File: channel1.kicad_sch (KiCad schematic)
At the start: 33 parts

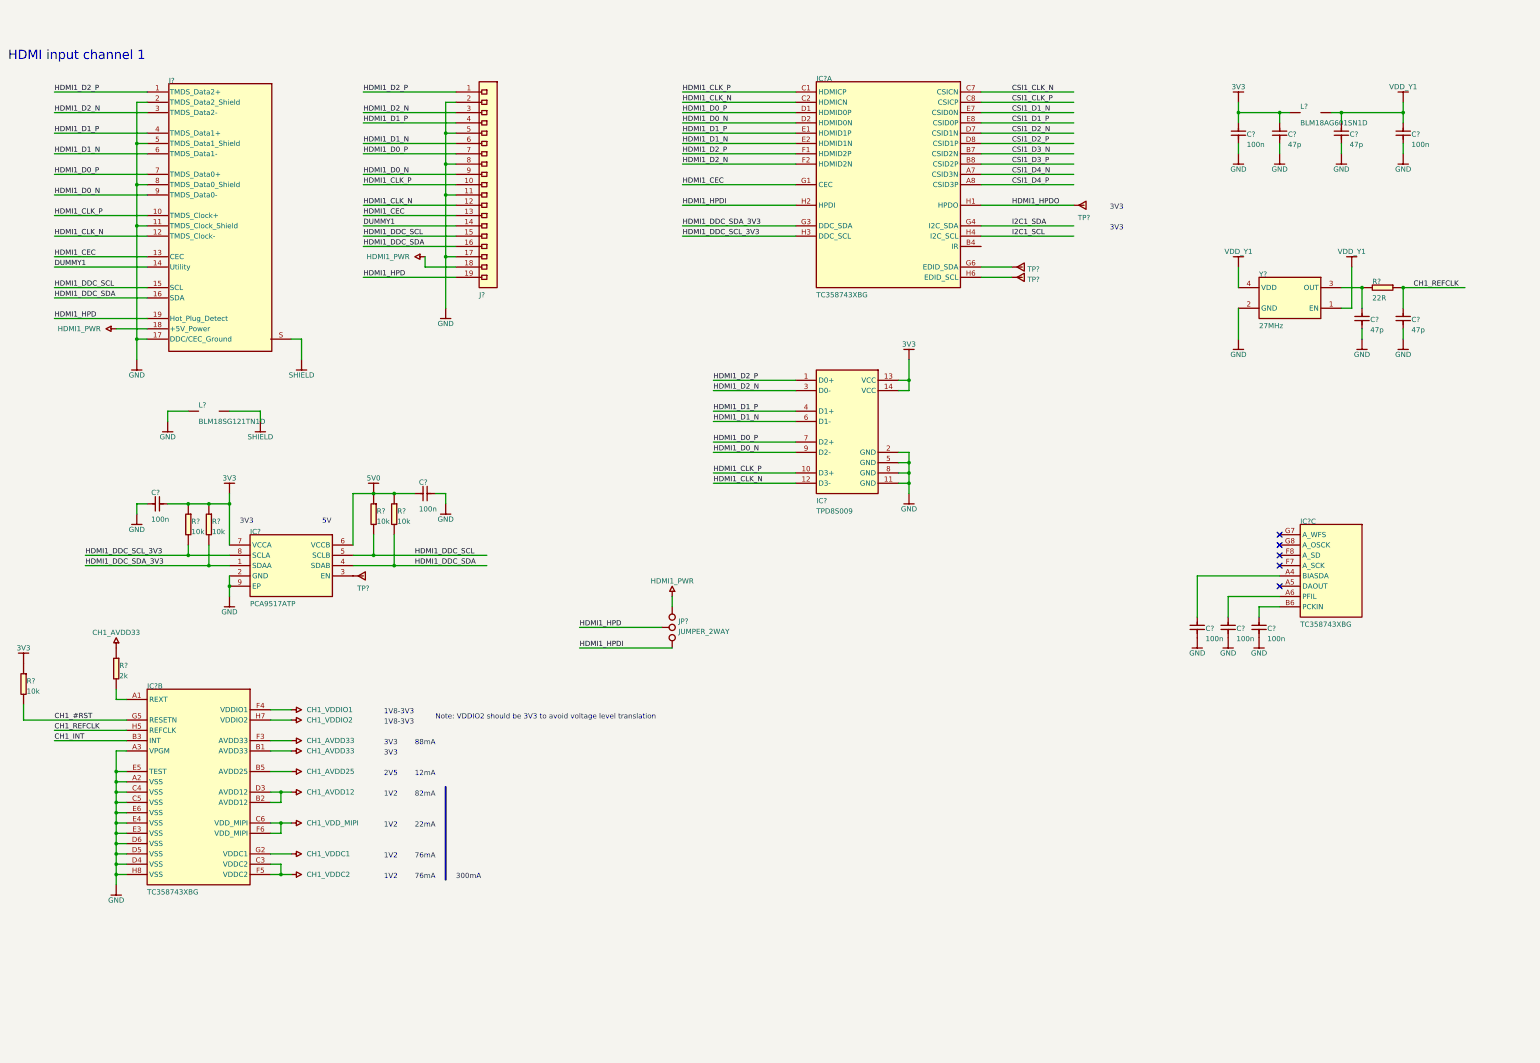
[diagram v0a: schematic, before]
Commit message: Change components to antmicro library ones
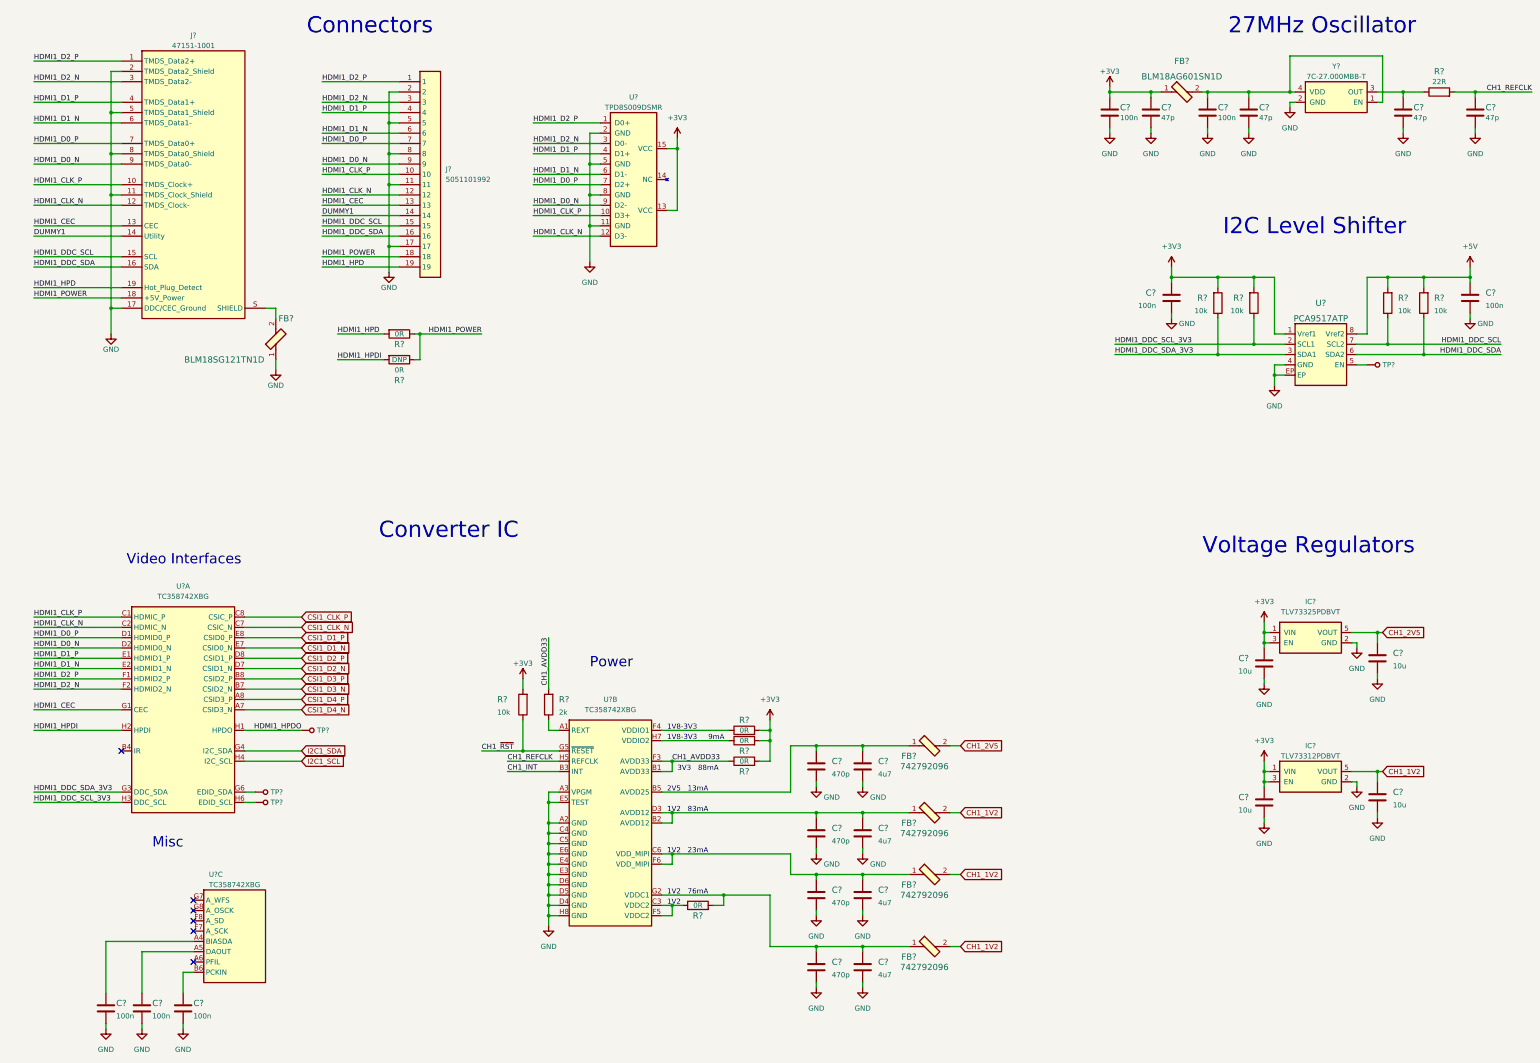
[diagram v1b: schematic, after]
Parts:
- removed C? (x9): ${ALTIUM_VALUE}, HDMI-MIPI-Bridge.Pcblib:0402, symbol altium_import-altium-import:1_C
- removed C? (x2): ${ALTIUM_VALUE}, HDMI-MIPI-Bridge.Pcblib:0402, symbol altium_import-altium-import:2_C
- removed IC? (x3): ${ALTIUM_VALUE}, HDMI-MIPI-Bridge.Pcblib:TC358743XBG, symbol altium_import-altium-import:0_TC358743XBG
- removed IC?: ${ALTIUM_VALUE}, HDMI-MIPI-Bridge.Pcblib:PCA9517ATP, symbol altium_import-altium-import:0_PCA9517ATP
- removed IC?: ${ALTIUM_VALUE}, HDMI-MIPI-Bridge.Pcblib:SON-15, symbol altium_import-altium-import:0_TPD8S009
- removed J?: ${ALTIUM_VALUE}, HDMI-MIPI-Bridge.Pcblib:Molex_HDMI_471511001, symbol altium_import-altium-import:0_CON-Molex-471511001
- removed J?: ${ALTIUM_VALUE}, HDMI-MIPI-Bridge.Pcblib:CON-Molex-505110-1992, symbol altium_import-altium-import:0_1X19
- removed JP?: JUMPER_2WAY, HDMI-MIPI-Bridge.Pcblib:JUMPER_2WAY, symbol altium_import-altium-import:3_JUMPER_2WAY
- removed L? (x2): ${ALTIUM_VALUE}, HDMI-MIPI-Bridge.Pcblib:0603, symbol altium_import-altium-import:0_Inductor SMT
- removed R?: ${ALTIUM_VALUE}, HDMI-MIPI-Bridge.Pcblib:0603, symbol altium_import-altium-import:1_R
- removed R? (x5): ${ALTIUM_VALUE}, HDMI-MIPI-Bridge.Pcblib:0402, symbol altium_import-altium-import:1_R
- removed R?: ${ALTIUM_VALUE}, HDMI-MIPI-Bridge.Pcblib:0402, symbol altium_import-altium-import:0_R
- removed TP? (x4): Testpad, HDMI-MIPI-Bridge.Pcblib:TP-R-1, symbol altium_import-altium-import:3_Testpad
- removed Y?: ${ALTIUM_VALUE}, HDMI-MIPI-Bridge.Pcblib:TXC_7C, symbol altium_import-altium-import:0_TXC_7C
- added C? (x4): C_4u7_0603, antmicro-footprints:0603-cap, symbol antmicroCapacitors0603:C_4u7_0603
- added C? (x4): C_470p_0402, antmicro-footprints:0402-cap, symbol antmicroCapacitors0402:C_470p_0402
- added C? (x4): C_10u_0603, antmicro-footprints:0603-cap, symbol antmicroCapacitors0603:C_10u_0603
- added C? (x7): C_100n_0402, antmicro-footprints:0402-cap, symbol antmicroCapacitors0402:C_100n_0402
- added C? (x4): C_47p_0402, antmicro-footprints:0402-cap, symbol antmicroCapacitors0402:C_47p_0402
- added FB? (x4): 742792096, antmicro-footprints:0805-res, symbol antmicroFerriteBeadsandChips:742792096
- added FB?: BLM18SG121TN1D, antmicro-footprints:0603-res, symbol antmicroFerriteBeadsandChips:BLM18SG121TN1D
- added FB?: BLM18AG601SN1D, antmicro-footprints:0603, symbol antmicroFerriteBeadsandChips:BLM18AG601SN1D
- added IC?: TLV73312PDBVT, antmicro-footprints:SOT-23-5, symbol antmicroPMICVoltageRegulatorsLinear:TLV73312PDBVT
- added IC?: TLV73325PDBVT, antmicro-footprints:SOT-23-5, symbol antmicroPMICVoltageRegulatorsLinear:TLV73325PDBVT
- added J?: 5051101992, antmicro-footprints:5051101992, symbol antmicroFCCConnectors:5051101992
- added J?: 47151-1001, antmicro-footprints:47151-1001, symbol antmicroUSBDVIHDMIConnectors:47151-1001
- added R? (x5): R_10k_0402, antmicro-footprints:0402-res, symbol antmicroResistors0402:R_10k_0402
- added R? (x6): R_0R_0603, antmicro-footprints:0603-res, symbol antmicroResistors0603:R_0R_0603
- added R?: R_22R_0402, antmicro-footprints:0402-res, symbol antmicroResistors0402:R_22R_0402
- added R?: R_2k_0402, antmicro-footprints:0402-res, symbol antmicroResistors0402:R_2k_0402
- added TP? (x4): TP_SMD_0_75MM, antmicro-footprints:Testpoint_smd_0_75mm, symbol antmicroTestPoints:TP_SMD_0_75MM
- added U?: TPD8S009DSMR, antmicro-footprints:R-PDSO-N15, symbol antmicroTVSDiodes:TPD8S009DSMR
- added U?: PCA9517ATP, antmicro-footprints:SOT1069-2, symbol antmicroLogicTranslatorsLevelShifters:PCA9517ATP
- added U? (x3): TC358742XBG, antmicro-footprints:BGA-64_8x8_6.0x6.0mm, symbol antmicroInterfaceControllers:TC358742XBG
- added Y?: 7C-27.000MBB-T, antmicro-footprints:7C-24.000MBB-T, symbol antmicroOscillators:7C-27.000MBB-T
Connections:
- net CH1_AVDD33: now also R?.1, R?.2, U?.B1 (AVDD33), U?.F3 (AVDD33)
- net CH1_INT: now also U?.B3 (INT)
- net CH1_REFCLK: now also C?.1, R?.2, U?.H5 (REFCLK)
- net CSI1_CLK_N: now also U?.C7 (CSIC_N)
- net CSI1_CLK_P: now also U?.C8 (CSIC_P)
- net CSI1_D1_N: now also U?.E7 (CSID0_N)
- net CSI1_D1_P: now also U?.E8 (CSID0_P)
- net CSI1_D2_N: now also U?.D7 (CSID1_N)
- net CSI1_D2_P: now also U?.D8 (CSID1_P)
- net CSI1_D3_N: now also U?.B7 (CSID2_N)
- net CSI1_D3_P: now also U?.B8 (CSID2_P)
- net CSI1_D4_N: now also U?.A7 (CSID3_N)
- net CSI1_D4_P: now also U?.A8 (CSID3_P)
- net DUMMY1: now also J?.14, J?.14 (Utility)
- net GND: now also C?.1, C?.1, C?.1, C?.1, C?.2, C?.2, C?.2, C?.2, C?.2, C?.2, C?.2, C?.2, C?.2, C?.2, C?.2, C?.2, C?.2, C?.2, C?.2, C?.2, C?.2, C?.2, C?.2, FB?.1, IC?.2 (GND), IC?.2 (GND), J?.11, J?.11 (TMDS_Clock_Shield), J?.17, J?.17 (DDC/CEC_Ground), J?.2, J?.2 (TMDS_Data2_Shield), J?.5, J?.5 (TMDS_Data1_Shield), J?.8, J?.8 (TMDS_Data0_Shield), U?.11 (GND), U?.2 (GND), U?.4 (GND), U?.5 (GND), U?.8 (GND), U?.A2 (GND), U?.A3 (VPGM), U?.C4 (GND), U?.C5 (GND), U?.D4 (GND), U?.D5 (GND), U?.D6 (GND), U?.E3 (GND), U?.E4 (GND), U?.E5 (TEST), U?.E6 (GND), U?.EP, U?.H8 (GND), Y?.2 (GND)
- net HDMI1_CEC: now also J?.13, J?.13 (CEC), U?.G1 (CEC)
- net HDMI1_CLK_N: now also J?.12, J?.12 (TMDS_Clock-), U?.12 (D3-), U?.C2 (HDMIC_N)
- net HDMI1_CLK_P: now also J?.10, J?.10 (TMDS_Clock+), U?.10 (D3+), U?.C1 (HDMIC_P)
- net HDMI1_D0_N: now also J?.9, J?.9 (TMDS_Data0-), U?.9 (D2-), U?.D2 (HDMID0_N)
- net HDMI1_D0_P: now also J?.7, J?.7 (TMDS_Data0+), U?.7 (D2+), U?.D1 (HDMID0_P)
- net HDMI1_D1_N: now also J?.6, J?.6 (TMDS_Data1-), U?.6 (D1-), U?.E2 (HDMID1_N)
- net HDMI1_D1_P: now also J?.4, J?.4 (TMDS_Data1+), U?.4 (D1+), U?.E1 (HDMID1_P)
- net HDMI1_D2_N: now also J?.3, J?.3 (TMDS_Data2-), U?.3 (D0-), U?.F2 (HDMID2_N)
- net HDMI1_D2_P: now also J?.1, J?.1 (TMDS_Data2+), U?.1 (D0+), U?.F1 (HDMID2_P)
- net HDMI1_DDC_SCL: now also J?.15, J?.15 (SCL), R?.1, U?.7 (SCL2)
- net HDMI1_DDC_SCL_3V3: now also R?.1, U?.2 (SCL1), U?.H3 (DDC_SCL)
- net HDMI1_DDC_SDA: now also J?.16, J?.16 (SDA), R?.1, U?.6 (SDA2)
- net HDMI1_DDC_SDA_3V3: now also R?.1, U?.3 (SDA1), U?.G3 (DDC_SDA)
- net HDMI1_HPD: now also J?.19, J?.19 (Hot_Plug_Detect), R?.2
- net HDMI1_HPDI: now also R?.2, U?.H2 (HPDI)
- net HDMI1_HPDO: now also TP?.1, U?.H1 (HPDO)
- net I2C1_SCL: now also U?.H4 (I2C_SCL)
- net I2C1_SDA: now also U?.G4 (I2C_SDA)
- new net: C?.1, C?.2, FB?.1, U?.C6 (VDD_MIPI), U?.F6 (VDD_MIPI)
- new net: C?.1, C?.2, FB?.1, R?.2, U?.G2 (VDDC1)
- new net: R?.1, U?.F4 (VDDIO1)
- new net: R?.1, U?.C3 (VDDC2), U?.F5 (VDDC2)
- new net: C?.1, U?.A4 (BIASDA)
- new net: C?.1, C?.2, FB?.1, U?.B5 (AVDD25)
- new net: C?.1, C?.1, FB?.2, Y?.1 (EN), Y?.4 (VDD)
- new net: TP?.1, U?.5 (EN)
- new net: C?.1, U?.B6 (PCKIN)
- new net: C?.1, R?.1, Y?.3 (OUT)
- new net: C?.1, U?.A5 (DAOUT)
- new net: FB?.2, J?.S (SHIELD)
- new net: TP?.1, U?.G6 (EDID_SDA)
- new net: TP?.1, U?.H6 (EDID_SCL)
- new net: C?.1, C?.2, FB?.1, U?.B2 (AVDD12), U?.D3 (AVDD12)
- new net: R?.1, U?.H7 (VDDIO2)
- new net: R?.1, U?.A1 (REXT)
- new net +3V3: C?.1, C?.1, C?.1, C?.1, C?.1, FB?.1, IC?.1 (VIN), IC?.1 (VIN), IC?.3 (EN), IC?.3 (EN), R?.2, R?.2, R?.2, R?.2, R?.2, R?.2, U?.1 (Vref1), U?.13 (VCC), U?.15 (VCC)
- new net +5V: C?.1, R?.2, R?.2, U?.8 (Vref2)
- new net CH1_1V2: C?.1, FB?.2, FB?.2, FB?.2, IC?.5 (VOUT)
- new net CH1_2V5: C?.1, FB?.2, IC?.5 (VOUT)
- new net CH1_~{RST}: R?.1, U?.G5 (~{RESET})
- new net HDMI1_POWER: J?.18, J?.18 (+5V_Power), R?.1, R?.1
- no-connect marks 5 -> 6
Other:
- note added: "13mA"
- note added: "23mA"
- note added: "27MHz Oscillator"
- note added: "83mA"
- note added: "9mA"
- note added: "Connectors"
- note added: "Converter IC"
- note added: "I2C Level Shifter"
- note added: "Misc"
- note added: "Power"
- note added: "Video Interfaces"
- note added: "Voltage Regulators"
- note removed: "12mA"
- note removed: "22mA"
- note removed: "300mA"
- note removed: "5V"
- note removed: "82mA"
- note removed: "HDMI input channel 1"
- note removed: "Note: VDDIO2 should be 3V3 to avoid voltage level translation"

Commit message: Layout of the PCB
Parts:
- removed R? (x2): R_0R_0603, antmicro-footprints:0603-res, symbol antmicroResistors0603:R_0R_0603
- added C27, C28, C29, C30: C_100n_0402, antmicro-footprints:0402-cap, symbol antmicroCapacitors0402:C_100n_0402
- added R6, R7: R_0R_0603, antmicro-footprints:0603-res, symbol antmicroResistors0603:R_0R_0603
- C13, C21, C23: renamed from C?; DNP (none) -> DNP
- gave numbers to parts that had none: 49
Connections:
- net +3V3: now also R6.2, R7.2
- net CH1_AVDD33: now also C30.1
- net GND: now also C27.2, C28.2, C29.2, C30.2
- net at U1.F4 (VDDIO1): now also C28.1, R6.1
- net at R5.1, U1.C3 (VDDC2), U1.F5 (VDDC2): now also C27.1
- net at U1.H7 (VDDIO2): now also C29.1, R7.1
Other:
- moved on the sheet: C10, C11, C4, C5, C6, C7, C8, C9, FB2, FB3, FB4, FB5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

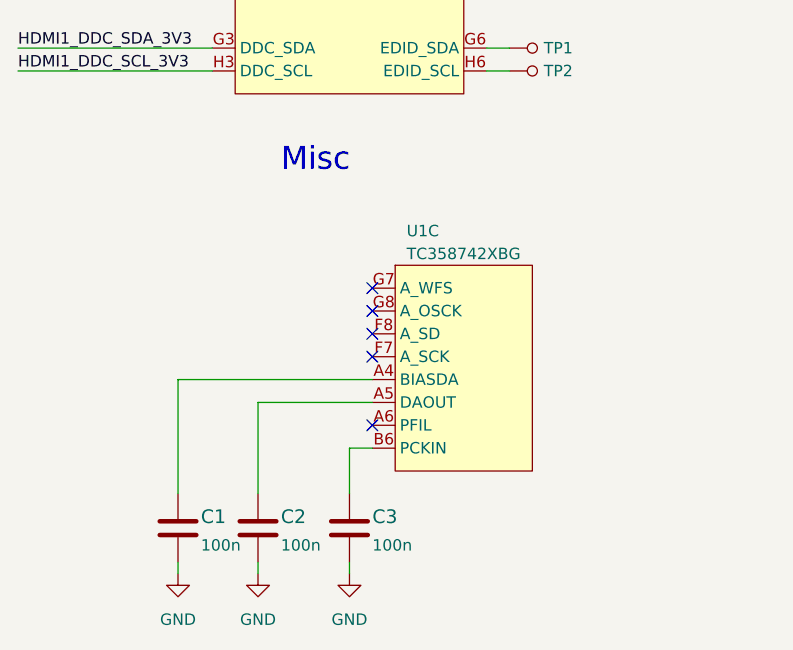
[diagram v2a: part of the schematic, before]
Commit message: Added logos
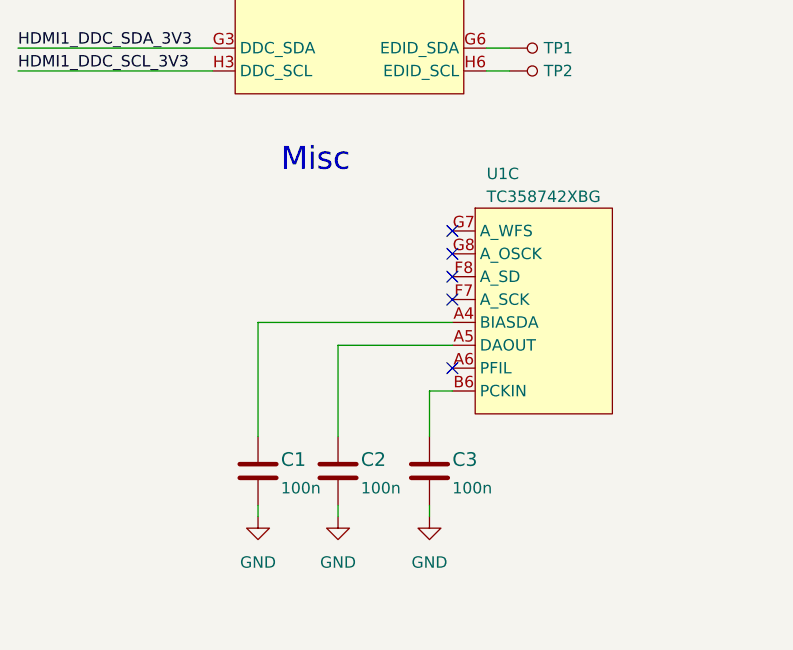
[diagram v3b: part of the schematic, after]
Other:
- moved on the sheet: C1, C2, C3, U1C

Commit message: Schematic cleanup
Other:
- moved on the sheet: C1, C10, C11, C2, C27, C28, C29, C3, C30, C4, C5, C6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

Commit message: Update local library of components
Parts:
- C1, C12, C14, C15, C2, C22, C27, C28, C29, C3, C30: footprint antmicro-footprints:0402-cap -> antmicro-hdmi-mipi-bridge-hw-footprints:0402-cap; symbol antmicroCapacitors0402:C_100n_0402 -> antmicro-hdmi-mipi-bridge-hw:C_100n_0402
- C10, C11, C8, C9: footprint antmicro-footprints:0603-cap -> antmicro-hdmi-mipi-bridge-hw-footprints:0603-cap; symbol antmicroCapacitors0603:C_4u7_0603 -> antmicro-hdmi-mipi-bridge-hw:C_4u7_0603
- C13, C16, C21, C23: footprint antmicro-footprints:0402-cap -> antmicro-hdmi-mipi-bridge-hw-footprints:0402-cap; symbol antmicroCapacitors0402:C_47p_0402 -> antmicro-hdmi-mipi-bridge-hw:C_47p_0402
- C17, C18, C19, C20: footprint antmicro-footprints:0603-cap -> antmicro-hdmi-mipi-bridge-hw-footprints:0603-cap; symbol antmicroCapacitors0603:C_10u_0603 -> antmicro-hdmi-mipi-bridge-hw:C_10u_0603
- C4, C5, C6, C7: footprint antmicro-footprints:0402-cap -> antmicro-hdmi-mipi-bridge-hw-footprints:0402-cap; symbol antmicroCapacitors0402:C_470p_0402 -> antmicro-hdmi-mipi-bridge-hw:C_470p_0402
- FB1: footprint antmicro-footprints:0603-res -> antmicro-hdmi-mipi-bridge-hw-footprints:0603-res; symbol antmicroFerriteBeadsandChips:BLM18SG121TN1D -> antmicro-hdmi-mipi-bridge-hw:BLM18SG121TN1D
- FB2, FB3, FB4, FB5: footprint antmicro-footprints:0805-res -> antmicro-hdmi-mipi-bridge-hw-footprints:0805-res; symbol antmicroFerriteBeadsandChips:742792096 -> antmicro-hdmi-mipi-bridge-hw:742792096
- FB6: footprint antmicro-footprints:0603 -> antmicro-hdmi-mipi-bridge-hw-footprints:0603; symbol antmicroFerriteBeadsandChips:BLM18AG601SN1D -> antmicro-hdmi-mipi-bridge-hw:BLM18AG601SN1D
- IC1: footprint antmicro-footprints:SOT-23-5 -> antmicro-hdmi-mipi-bridge-hw-footprints:SOT-23-5; symbol antmicroPMICVoltageRegulatorsLinear:TLV73325PDBVT -> antmicro-hdmi-mipi-bridge-hw:TLV73325PDBVT
- IC2: footprint antmicro-footprints:SOT-23-5 -> antmicro-hdmi-mipi-bridge-hw-footprints:SOT-23-5; symbol antmicroPMICVoltageRegulatorsLinear:TLV73312PDBVT -> antmicro-hdmi-mipi-bridge-hw:TLV73312PDBVT
- J2: footprint antmicro-footprints:47151-1001 -> antmicro-hdmi-mipi-bridge-hw-footprints:47151-1001; symbol antmicroUSBDVIHDMIConnectors:47151-1001 -> antmicro-hdmi-mipi-bridge-hw:47151-1001
- J3: footprint antmicro-footprints:5051101992 -> antmicro-hdmi-mipi-bridge-hw-footprints:5051101992; symbol antmicroFCCConnectors:5051101992 -> antmicro-hdmi-mipi-bridge-hw:5051101992
- R1, R2, R5, R6, R7, R8: footprint antmicro-footprints:0603-res -> antmicro-hdmi-mipi-bridge-hw-footprints:0603-res; symbol antmicroResistors0603:R_0R_0603 -> antmicro-hdmi-mipi-bridge-hw:R_0R_0603
- R10, R11, R12, R3, R9: footprint antmicro-footprints:0402-res -> antmicro-hdmi-mipi-bridge-hw-footprints:0402-res; symbol antmicroResistors0402:R_10k_0402 -> antmicro-hdmi-mipi-bridge-hw:R_10k_0402
- R13: footprint antmicro-footprints:0402-res -> antmicro-hdmi-mipi-bridge-hw-footprints:0402-res; symbol antmicroResistors0402:R_22R_0402 -> antmicro-hdmi-mipi-bridge-hw:R_22R_0402
- R4: footprint antmicro-footprints:0402-res -> antmicro-hdmi-mipi-bridge-hw-footprints:0402-res; symbol antmicroResistors0402:R_2k_0402 -> antmicro-hdmi-mipi-bridge-hw:R_2k_0402
- TP1, TP2, TP3, TP4: footprint antmicro-footprints:Testpoint_smd_0_75mm -> antmicro-hdmi-mipi-bridge-hw-footprints:Testpoint_smd_0_75mm; symbol antmicroTestPoints:TP_SMD_0_75MM -> antmicro-hdmi-mipi-bridge-hw:TP_SMD_0_75MM
- U1: footprint antmicro-footprints:BGA-64_8x8_6.0x6.0mm -> antmicro-hdmi-mipi-bridge-hw-footprints:BGA-64_8x8_6.0x6.0mm; symbol antmicroInterfaceControllers:TC358742XBG -> antmicro-hdmi-mipi-bridge-hw:TC358742XBG
- U2: footprint antmicro-footprints:R-PDSO-N15 -> antmicro-hdmi-mipi-bridge-hw-footprints:R-PDSO-N15; symbol antmicroTVSDiodes:TPD8S009DSMR -> antmicro-hdmi-mipi-bridge-hw:TPD8S009DSMR
- U3: footprint antmicro-footprints:SOT1069-2 -> antmicro-hdmi-mipi-bridge-hw-footprints:SOT1069-2; symbol antmicroLogicTranslatorsLevelShifters:PCA9517ATP -> antmicro-hdmi-mipi-bridge-hw:PCA9517ATP
- Y1: footprint antmicro-footprints:7C-24.000MBB-T -> antmicro-hdmi-mipi-bridge-hw-footprints:7C-24.000MBB-T; symbol antmicroOscillators:7C-27.000MBB-T -> antmicro-hdmi-mipi-bridge-hw:7C-27.000MBB-T
